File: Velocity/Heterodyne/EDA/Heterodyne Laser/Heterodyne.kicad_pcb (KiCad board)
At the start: 2 copper layers, 35.5 x 19 mm, 38 parts, among them J1 Conn_01x05, J7 Reciever, U1 SA612AD, U2 NE5532DR, U3 MAX7375AXR105, U4 MAX11613, U5 ATmega328PB-AU, Y1 8 MHz

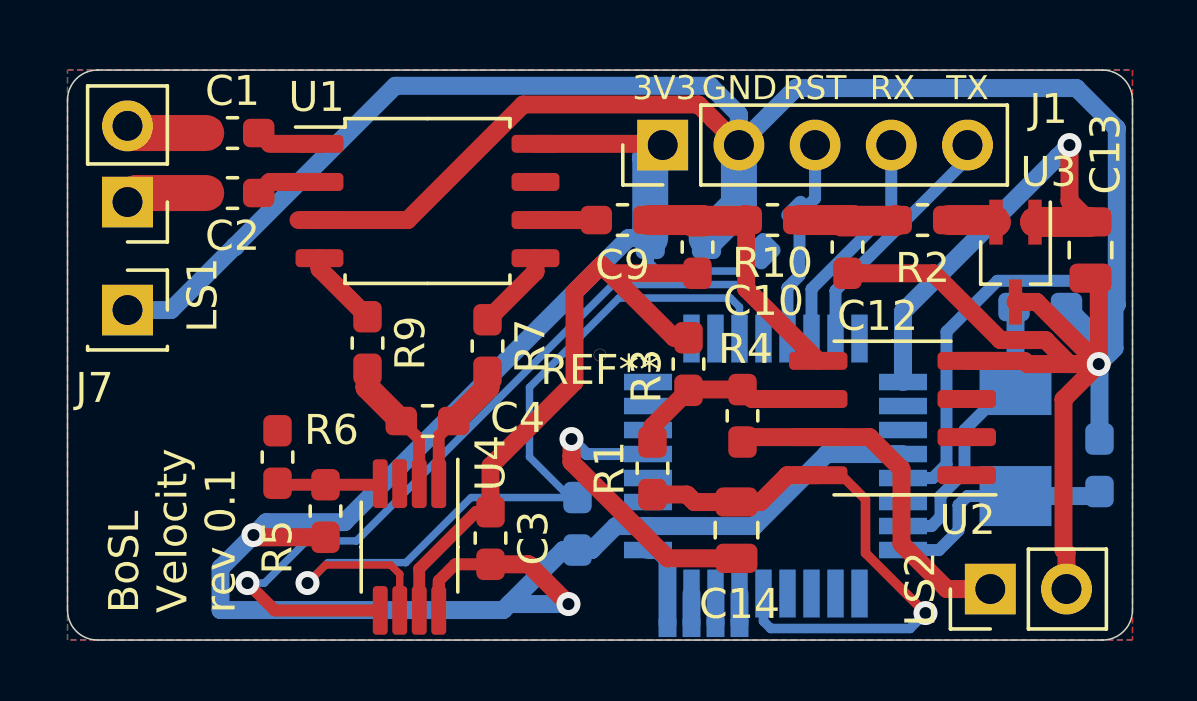
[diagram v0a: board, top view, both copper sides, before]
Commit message: added modifed designs for laser heterodyne pcb
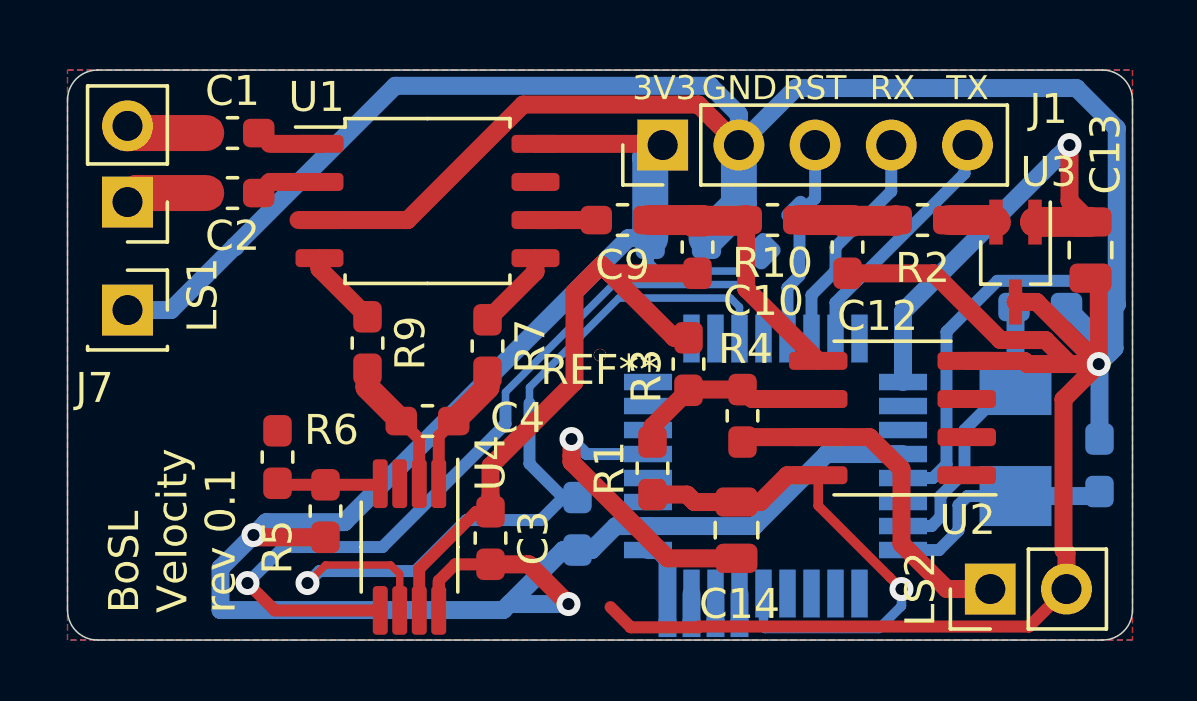
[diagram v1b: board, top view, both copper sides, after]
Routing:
- net GND: track 146.2 -> 162.2 mm
- net VOPAMP: track 19.7 -> 18.1 mm
- net SCL: track 27.5 -> 28.1 mm
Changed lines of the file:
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@@
     (thickness 1.6)
     (drawings 15)
-    (tracks 242)
+    (tracks 257)
     (zones 0)
     (modules 38)
@@
   )
   (setup
-    (last_trace_width 0.25)
+    (last_trace_width 0.4)
     (user_trace_width 0.32)
     (user_trace_width 0.4)
@@
     (user_trace_width 2.4)
     (trace_clearance 0.2)
-    (zone_clearance 0.25)
+    (zone_clearance 0.6)
     (zone_45_only no)
     (trace_min 0.2)
@@
     (aux_axis_origin 0 0)
     (grid_origin 137.9 56.7)
-    (visible_elements 7FFFFFFF)
+    (visible_elements 7FFFEFFF)
     (pcbplotparams
       (layerselection 0x010c0_ffffffff)
@@
   (via (at 16.8 12.3) (size 0.8) (drill 0.4) (layers F.Cu B.Cu) (net 1))
   (segment (start 19.35 12.8) (end 17.3 12.8) (width 0.4) (layer B.Cu) (net 1))
+  (segment (start 21.049999 18.550001) (end 21.02501 18.57499) (width 0.4) (layer F.Cu) (net 1))
+  (segment (start 33.3 17.3) (end 32.049999 18.550001) (width 0.4) (layer F.Cu) (net 1))
+  (segment (start 32.049999 18.550001) (end 21.049999 18.550001) (width 0.4) (layer F.Cu) (net 1))
+  (segment (start 21.02501 18.57499) (end 18.77499 18.57499) (width 0.4) (layer F.Cu) (net 1))
+  (segment (start 18.77499 18.57499) (end 18.1 17.9) (width 0.4) (layer F.Cu) (net 1))
   (segment (start 12.375 18.0125) (end 12.375 17.025) (width 0.4) (layer F.Cu) (net 2) (status 10))
   (segment (start 12.925 16.475) (end 14.1 16.475) (width 0.4) (layer F.Cu) (net 2) (status 20))
@@
   (segment (start 16.699999 17.800001) (end 16.7 17.8) (width 0.6) (layer B.Cu) (net 2))
   (segment (start 5.100017 16.599983) (end 6.2 15.5) (width 0.6) (layer B.Cu) (net 2))
-  (via (at 6.2 15.5) (size 0.8) (drill 0.4) (layers F.Cu B.Cu) (net 2) (status 1000000))
+  (via (at 6.2 15.5) (size 0.8) (drill 0.4) (layers F.Cu B.Cu) (net 2))
   (segment (start 14.524983 18.000017) (end 5.100017 18.000017) (width 0.6) (layer B.Cu) (net 2))
   (segment (start 5.100017 18.000017) (end 5.100017 16.599983) (width 0.6) (layer B.Cu) (net 2))
@@
   (segment (start 20.9 14.4) (end 20.65 14.15) (width 0.6) (layer F.Cu) (net 23))
   (segment (start 22 14.4) (end 22.3 14.4) (width 0.6) (layer F.Cu) (net 23) (status 30))
-  (via (at 28.6 18.1) (size 0.8) (drill 0.4) (layers F.Cu B.Cu) (net 23))
-  (segment (start 23.2 18.373002) (end 23.441988 18.61499) (width 0.32) (layer B.Cu) (net 23))
-  (segment (start 23.2 17.45) (end 23.2 18.373002) (width 0.32) (layer B.Cu) (net 23))
-  (segment (start 28.08501 18.61499) (end 28.6 18.1) (width 0.32) (layer B.Cu) (net 23))
-  (segment (start 23.441988 18.61499) (end 28.08501 18.61499) (width 0.32) (layer B.Cu) (net 23))
-  (segment (start 25.025 13.505) (end 25.795 13.505) (width 0.32) (layer F.Cu) (net 23))
-  (segment (start 25.795 13.505) (end 26.6 14.31) (width 0.32) (layer F.Cu) (net 23))
-  (segment (start 26.6 16.1) (end 28.6 18.1) (width 0.32) (layer F.Cu) (net 23))
-  (segment (start 26.6 14.31) (end 26.6 16.1) (width 0.32) (layer F.Cu) (net 23))
+  (via (at 27.8 17.3) (size 0.8) (drill 0.4) (layers F.Cu B.Cu) (net 23))
+  (segment (start 23.2 18.57) (end 23.24499 18.61499) (width 0.32) (layer B.Cu) (net 23))
+  (segment (start 23.24499 18.61499) (end 27.050695 18.61499) (width 0.32) (layer B.Cu) (net 23))
+  (segment (start 25.025 14.525) (end 27.400001 16.900001) (width 0.32) (layer F.Cu) (net 23))
+  (segment (start 27.8 17.865685) (end 27.8 17.3) (width 0.32) (layer B.Cu) (net 23))
+  (segment (start 27.400001 16.900001) (end 27.8 17.3) (width 0.32) (layer F.Cu) (net 23))
+  (segment (start 23.2 17.45) (end 23.2 18.57) (width 0.32) (layer B.Cu) (net 23))
+  (segment (start 27.050695 18.61499) (end 27.8 17.865685) (width 0.32) (layer B.Cu) (net 23))
+  (segment (start 25.025 13.505) (end 25.025 14.525) (width 0.32) (layer F.Cu) (net 23))
   (via (at 8 17.1) (size 0.8) (drill 0.4) (layers F.Cu B.Cu) (net 24))
   (segment (start 11.075 16.80001) (end 11.075 18.0125) (width 0.25) (layer F.Cu) (net 24))
@@
   (segment (start 8 17.1) (end 8.6 16.5) (width 0.25) (layer F.Cu) (net 24))
   (segment (start 8.6 16.5) (end 10.77499 16.5) (width 0.25) (layer F.Cu) (net 24))
-  (segment (start 13.45 14.25) (end 17 14.25) (width 0.25) (layer B.Cu) (net 24))
-  (segment (start 11.280553 16.419447) (end 13.45 14.25) (width 0.25) (layer B.Cu) (net 24))
-  (segment (start 8 17.1) (end 8.680553 16.419447) (width 0.25) (layer B.Cu) (net 24))
-  (segment (start 8.680553 16.419447) (end 11.280553 16.419447) (width 0.25) (layer B.Cu) (net 24))
   (segment (start 22.4 7.9) (end 22.4 8.95) (width 0.25) (layer B.Cu) (net 24))
   (segment (start 22.1 7.6) (end 22.4 7.9) (width 0.25) (layer B.Cu) (net 24))
-  (segment (start 16.75 14.25) (end 15.4 12.9) (width 0.25) (layer B.Cu) (net 24))
   (segment (start 17 14.25) (end 16.75 14.25) (width 0.25) (layer B.Cu) (net 24))
-  (segment (start 15.4 12.9) (end 15.4 10.575) (width 0.25) (layer B.Cu) (net 24))
   (segment (start 15.4 10.575) (end 18.375 7.6) (width 0.25) (layer B.Cu) (net 24))
   (segment (start 18.375 7.6) (end 22.1 7.6) (width 0.25) (layer B.Cu) (net 24))
+  (segment (start 15.4 10.575) (end 15.4 11.1) (width 0.25) (layer B.Cu) (net 24))
+  (segment (start 16.525 14.25) (end 17 14.25) (width 0.4) (layer B.Cu) (net 24))
+  (segment (start 15.4 13.125) (end 16.525 14.25) (width 0.4) (layer B.Cu) (net 24))
+  (segment (start 15.4 11.1) (end 15.4 13.125) (width 0.4) (layer B.Cu) (net 24))
+  (segment (start 8.4 16.7) (end 8 17.1) (width 0.4) (layer B.Cu) (net 24))
+  (segment (start 11.6 16.7) (end 8.4 16.7) (width 0.4) (layer B.Cu) (net 24))
+  (segment (start 13.3 15) (end 11.6 16.7) (width 0.4) (layer B.Cu) (net 24))
+  (segment (start 16.525 14.25) (end 15.775 15) (width 0.4) (layer B.Cu) (net 24))
+  (segment (start 15.775 15) (end 13.3 15) (width 0.4) (layer B.Cu) (net 24))
   (segment (start 6.912518 18.0125) (end 6.000018 17.1) (width 0.4) (layer F.Cu) (net 25))
   (segment (start 10.425 18.0125) (end 6.912518 18.0125) (width 0.4) (layer F.Cu) (net 25))
   (via (at 6.000018 17.1) (size 0.8) (drill 0.4) (layers F.Cu B.Cu) (net 25))
-  (segment (start 6.565703 17.1) (end 6.000018 17.1) (width 0.25) (layer B.Cu) (net 25))
-  (segment (start 7.971257 15.694446) (end 6.565703 17.1) (width 0.25) (layer B.Cu) (net 25))
+  (segment (start 6.000018 17.1) (end 7.200018 15.9) (width 0.4) (layer B.Cu) (net 25))
+  (segment (start 7.200018 15.9) (end 10.5 15.9) (width 0.4) (layer B.Cu) (net 25))
+  (segment (start 10.5 15.9) (end 14.6 11.8) (width 0.4) (layer B.Cu) (net 25))
+  (segment (start 14.6 11.8) (end 14.6 11.2) (width 0.4) (layer B.Cu) (net 25))
+  (segment (start 14.6 10.73859) (end 14.6 11.2) (width 0.25) (layer B.Cu) (net 25))
+  (segment (start 22.449991 7.149991) (end 18.175009 7.149991) (width 0.25) (layer B.Cu) (net 25))
   (segment (start 23.2 7.9) (end 22.449991 7.149991) (width 0.25) (layer B.Cu) (net 25))
+  (segment (start 18.175009 7.149991) (end 18.175009 7.163581) (width 0.25) (layer B.Cu) (net 25))
   (segment (start 23.2 8.95) (end 23.2 7.9) (width 0.25) (layer B.Cu) (net 25))
-  (segment (start 22.449991 7.149991) (end 18.175009 7.149991) (width 0.25) (layer B.Cu) (net 25))
-  (segment (start 9.630554 15.694446) (end 7.971257 15.694446) (width 0.25) (layer B.Cu) (net 25))
-  (segment (start 18.175009 7.149991) (end 9.630554 15.694446) (width 0.25) (layer B.Cu) (net 25))
+  (segment (start 18.175009 7.163581) (end 14.6 10.73859) (width 0.25) (layer B.Cu) (net 25))
   (segment (start 30 2.948542) (end 30 2.5) (width 0.4) (layer B.Cu) (net 27) (status 30))
-  (segment (start 25.6 8.95) (end 25.6 7.348542) (width 0.4) (layer B.Cu) (net 27) (status 10))
-  (segment (start 25.6 7.348542) (end 30 2.948542) (width 0.4) (layer B.Cu) (net 27) (status 20))
-  (segment (start 24.8 7.3) (end 24.8 8.95) (width 0.4) (layer B.Cu) (net 28) (status 20))
-  (segment (start 27.46 4.64) (end 24.8 7.3) (width 0.4) (layer B.Cu) (net 28))
-  (segment (start 27.46 2.5) (end 27.46 4.64) (width 0.4) (layer B.Cu) (net 28) (status 10))
+  (segment (start 25.6 7.75) (end 29.9 3.45) (width 0.4) (layer B.Cu) (net 27))
+  (segment (start 25.6 8.95) (end 25.6 7.75) (width 0.4) (layer B.Cu) (net 27))
+  (segment (start 29.9 2.6) (end 30 2.5) (width 0.4) (layer B.Cu) (net 27))
+  (segment (start 29.9 3.45) (end 29.9 2.6) (width 0.4) (layer B.Cu) (net 27))
+  (segment (start 24.8 8.95) (end 24.8 7.5) (width 0.4) (layer B.Cu) (net 28))
+  (segment (start 24.8 7.5) (end 25.6 6.7) (width 0.4) (layer B.Cu) (net 28))
+  (segment (start 25.6 6.7) (end 25.6 5.9) (width 0.4) (layer B.Cu) (net 28))
+  (segment (start 27.46 4.04) (end 27.46 2.5) (width 0.4) (layer B.Cu) (net 28))
+  (segment (start 25.6 5.9) (end 27.46 4.04) (width 0.4) (layer B.Cu) (net 28))
   (segment (start 24.92 4.28) (end 24.4 4.8) (width 0.4) (layer B.Cu) (net 39) (status 20))
   (segment (start 24.92 2.5) (end 24.92 4.28) (width 0.4) (layer B.Cu) (net 39) (status 10))
@@
   (segment (start 20 16.3) (end 20 18.47499) (width 0.6) (layer B.Cu) (net 47) (status 20))
   (zone (net 1) (net_name GND) (layer F.Cu) (hatch edge 0.508)
-    (connect_pads (clearance 0.25))
-    (min_thickness 0.5)
+    (connect_pads (clearance 0.6))
+    (min_thickness 0.4)
     (fill yes (arc_segments 32) (thermal_gap 0.508) (thermal_bridge_width 0.508))
     (polygon
@@
   )
   (zone (net 1) (net_name GND) (layer B.Cu) (hatch edge 0.508)
-    (connect_pads (clearance 0.25))
-    (min_thickness 0.25)
+    (connect_pads (clearance 0.6))
+    (min_thickness 0.4)
     (fill yes (arc_segments 32) (thermal_gap 0.508) (thermal_bridge_width 0.508))
     (polygon
@@
       )
     )
+  )
+  (zone (net 0) (net_name "") (layer B.Cu) (hatch edge 0.508)
+    (connect_pads (clearance 0.6))
+    (min_thickness 0.4)
+    (keepout (tracks allowed) (vias allowed) (copperpour not_allowed))
+    (fill (arc_segments 32) (thermal_gap 0.508) (thermal_bridge_width 0.508))
+    (polygon
+      (pts
+        (xy 24 4.3) (xy 22.1 6.3) (xy 20.3 6.3) (xy 20.3 3.2) (xy 24 3.2)
+      )
+    )
